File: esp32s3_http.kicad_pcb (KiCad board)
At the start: 2 copper layers, 55 x 90 mm, 30 parts, among them J1 USB_B, J2 Jack-DC, SW1 SW_Push, SW2 SW_Push, U1 ESP32-S3-WROOM-1, U2 LF33_TO220, U3 LF50_TO220, Y1 32.768KHz

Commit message: PCB: 回路図から更新 (F8, KiCad GUI)
Co-Authored-By: Claude Opus 5.5 <noreply@anthropic.com>
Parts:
- added J3: UART0, Connector_PinHeader_2.54mm:PinHeader_1x03_P2.54mm_Vertical, F.Cu at (88.5, 103.5)
- C1: value 22uF -> 22uF/10V; footprint Capacitor_SMD:C_0603_1608Metric_Pad1.08x0.95mm_HandSolder -> Capacitor_SMD:C_0805_2012Metric_Pad1.18x1.45mm_HandSolder
- C8: value 3.3uF -> 47uF/10V Ta; footprint Capacitor_SMD:C_0603_1608Metric_Pad1.08x0.95mm_HandSolder -> Capacitor_Tantalum_SMD:CP_EIA-3528-21_Kemet-B_HandSolder
- D1, D2, D3: value D -> 1N5819; footprint Diode_SMD:D_0603_1608Metric_Pad1.05x0.95mm_HandSolder -> Diode_THT:D_DO-41_SOD81_P7.62mm_Horizontal
- U2: value LF33_TO220 -> LM2940T-3.3
- U3: value LF50_TO220 -> NJM7805FA; footprint Package_TO_SOT_THT:TO-220-3_Vertical -> Package_TO_SOT_THT:TO-220F-3_Vertical
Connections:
- C8 pad 1: GND -> VDD33
- C8 pad 2: VDD33 -> GND
- U1 pad 15: SD_CS -> unconnected-(U1-IO3-Pad15)
- U1 pad 16: SD_SCK -> unconnected-(U1-IO46-Pad16)
- U1 pad 17: SD_MOSI -> SD_CS
- U1 pad 18: SD_MISO -> SD_SCK
- U1 pad 19: unconnected-(U1-IO11-Pad19) -> SD_MOSI
- U1 pad 20: unconnected-(U1-IO12-Pad20) -> SD_MISO
- U1 pad 36: unconnected-(U1-RXD0-Pad36) -> U0RXD
- U1 pad 37: unconnected-(U1-TXD0-Pad37) -> U0TXD

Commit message: PCB: 配置見直し、Freerouting による初回配線 (WIP)
Co-Authored-By: Claude Opus 5.5 <noreply@anthropic.com>
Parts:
- moved U6 45.6 mm to (60.5, 142.9), turned to 180 degrees
- moved D1 14.7 mm to (68.6, 121.5)
- moved U3 9.06 mm to (63.1, 122.6), turned to 180 degrees
- moved C9 8.94 mm to (63.6, 119.3), turned to 0 degrees
- moved D2 7.74 mm to (64.0, 112.3)
- moved C4 7.23 mm to (57.5, 109.3), turned to 0 degrees
- moved C8 6.74 mm to (68.5, 109.5)
- moved D3 6.43 mm to (64.0, 116.3), turned to 180 degrees
- moved C10 5.86 mm to (57.5, 119.3)
- moved H2 4.96 mm to (89.0, 68.6)
- moved U2 4.94 mm to (58.5, 106.0)
- moved J3 1.06 mm to (89.6, 103.5)
- renumbered REF** to H1, REF** to H2, REF** to H3, REF** to H4
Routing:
- net BOOT: track 53.4 -> 72.3 mm
- net JACK5V: track 25.8 -> 7.27 mm
- net Net-(D1-K): track 24.8 -> 9.85 mm
- net Net-(D1-A): track 4.75 -> 17.7 mm
- net W5500_CS: track 37.9 -> 44.5 mm, vias 0 -> 1
- net U0TXD: track 0.00 -> 5.56 mm
- net EN: track 52.3 -> 46.9 mm, vias 2 -> 0
- net U0RXD: track 0.00 -> 4.95 mm
- net 5V: track 42.4 -> 37.8 mm
- net SD_MOSI: track 35.5 -> 32.8 mm
- net SD_MISO: track 34.9 -> 32.2 mm
- net SD_SCK: track 35.8 -> 33.4 mm
- net DM: track 39.6 -> 42.0 mm, vias 0 -> 1
- net VDD33: track 96.5 -> 98.7 mm, vias 2 -> 0
- net W5500_NT: track 34.0 -> 36.1 mm, vias 0 -> 1
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
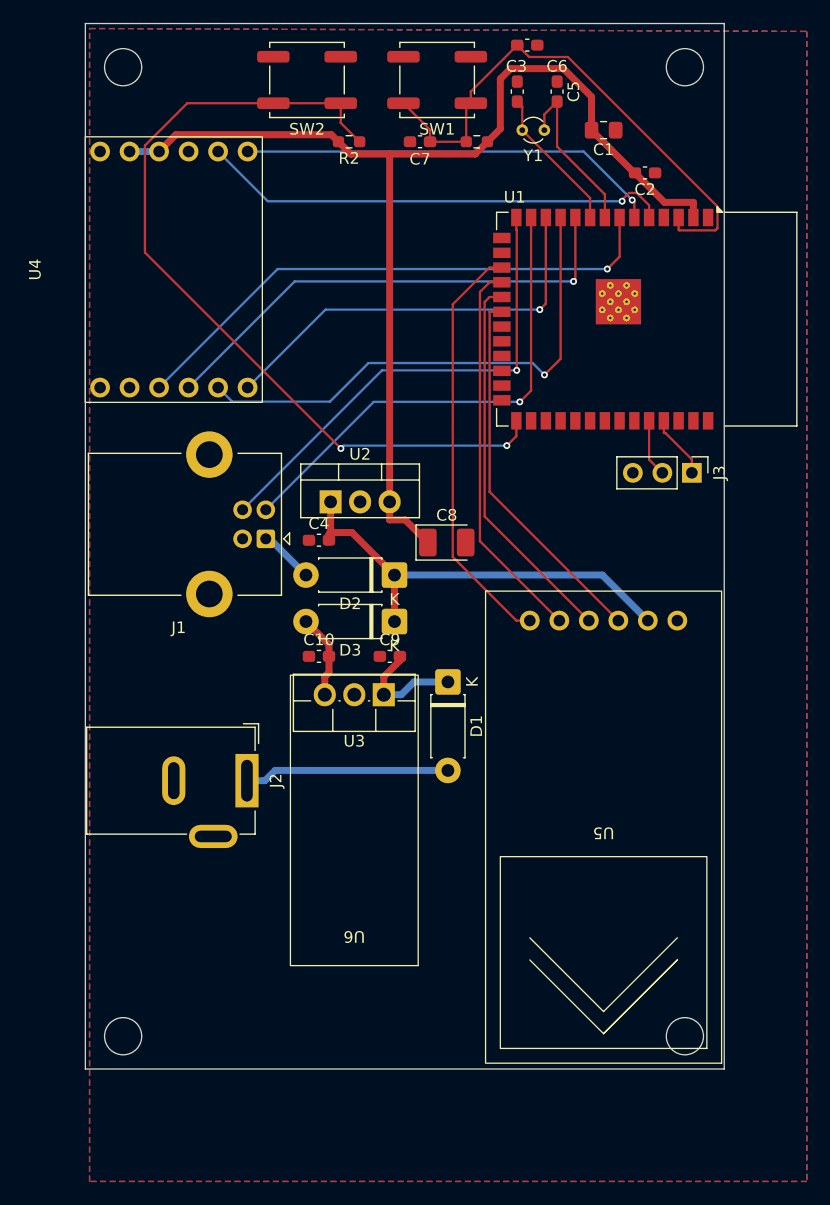
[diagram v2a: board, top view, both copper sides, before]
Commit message: PCB: W5500/SD のピン割当を配線向きに変更、EN/デカップリング集約、GND ステッチング
- W5500: IO9-IO14 (U1 左辺), SD: IO38-IO41 (U1 下辺, U5 直上)
- C2 を U1 pin1/2 直上に、EN 回路を pin3 直上に集約
- U1 EPAD サーマルビア 0.2 -> 0.3mm
- Power/GND ネットクラス (0.6mm) 追加

Co-Authored-By: Claude Opus 5.5 <noreply@anthropic.com>
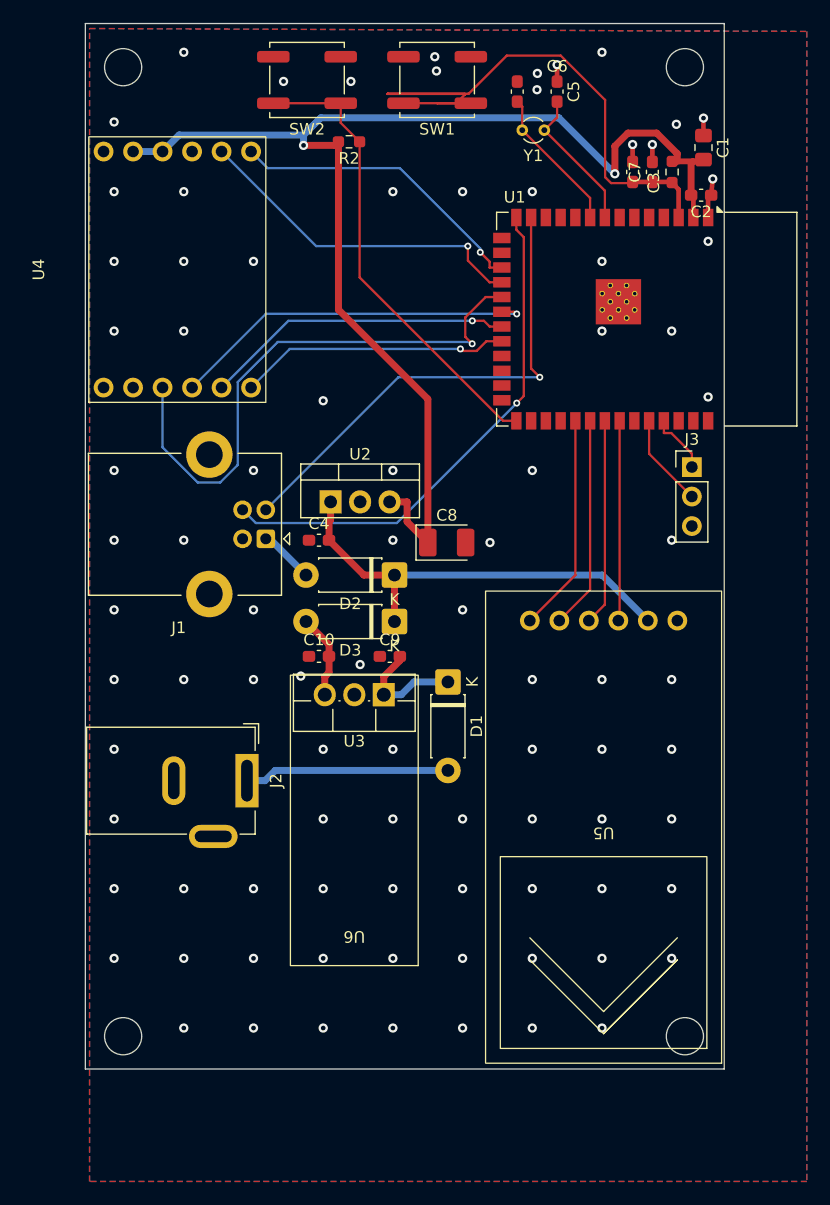
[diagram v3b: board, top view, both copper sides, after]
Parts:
- moved C7 20.2 mm to (86.2, 77.6), turned to -90 degrees
- moved R1 17.0 mm to (87.9, 77.6), turned to -90 degrees
- moved C3 14.2 mm to (84.5, 77.6), turned to -90 degrees
- moved C1 8.73 mm to (90.6, 75.5), turned to -90 degrees
- moved C2 5.20 mm to (90.4, 79.6)
- moved J3 0.50 mm to (89.6, 103.0), turned to 0 degrees
- moved U4 0.30 mm to (33.9, 86.0)
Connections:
- U1 pad 10: W5500_SCK -> unconnected-(U1-IO17-Pad10)
- U1 pad 11: W5500_CS -> unconnected-(U1-IO18-Pad11)
- U1 pad 12: W5500_NT -> unconnected-(U1-IO8-Pad12)
- U1 pad 17: SD_CS -> W5500_MOSI
- U1 pad 18: SD_SCK -> W5500_RST
- U1 pad 19: SD_MOSI -> W5500_MISO
- U1 pad 20: SD_MISO -> W5500_SCK
- U1 pad 21: unconnected-(U1-IO13-Pad21) -> W5500_CS
- U1 pad 22: unconnected-(U1-IO14-Pad22) -> W5500_NT
- U1 pad 31: unconnected-(U1-IO38-Pad31) -> SD_CS
- U1 pad 32: unconnected-(U1-IO39-Pad32) -> SD_SCK
- U1 pad 33: unconnected-(U1-IO40-Pad33) -> SD_MOSI
- U1 pad 34: unconnected-(U1-IO41-Pad34) -> SD_MISO
- U1 pad 5: W5500_RST -> unconnected-(U1-IO5-Pad5)
- U1 pad 6: W5500_MOSI -> unconnected-(U1-IO6-Pad6)
- U1 pad 7: W5500_MISO -> unconnected-(U1-IO7-Pad7)
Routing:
- net BOOT: track 72.3 -> 40.1 mm, vias 2 -> 0
- net W5500_CS: track 44.5 -> 26.7 mm
- net SD_CS: track 36.2 -> 18.8 mm
- net SD_SCK: track 33.4 -> 18.3 mm
- net SD_MOSI: track 32.8 -> 17.8 mm
- net SD_MISO: track 32.2 -> 17.2 mm
- net W5500_NT: track 36.1 -> 23.4 mm
- net W5500_RST: track 40.7 -> 29.5 mm
- net VDD33: track 98.7 -> 109.7 mm, vias 0 -> 2
- net W5500_SCK: track 42.5 -> 31.9 mm
- net W5500_MOSI: track 36.4 -> 26.2 mm
- net GND: track 0.00 -> 9.54 mm, vias 0 -> 89
- net EN: track 46.9 -> 54.5 mm
- net DP: track 41.7 -> 44.8 mm
- net U0RXD: track 4.95 -> 8.04 mm
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
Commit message: PCB: 配線完了、シルク整理
- W5500 バス・VDD33 幹線・EN/デカップリングを固定配線、残りを Freerouting で配線
- GND ステッチングビア、値表示を F.Fab へ、リファレンス位置調整
- DRC: 未配線 0、電気的違反 0 (残りは U3/U6 重ね置き等の意図的なもの)

Co-Authored-By: Claude Opus 5.5 <noreply@anthropic.com>
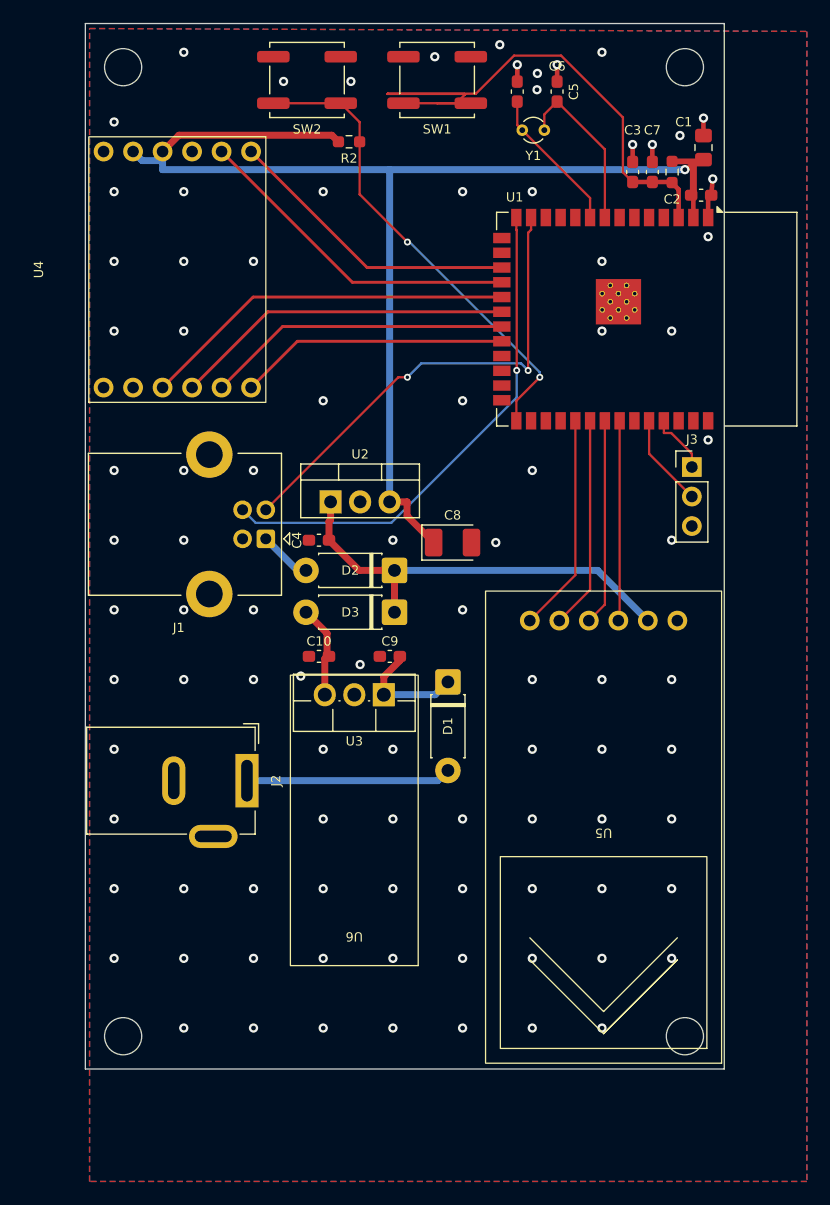
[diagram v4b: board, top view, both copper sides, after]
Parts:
- moved D3 0.80 mm to (64.0, 115.5)
- moved C8 0.50 mm to (69.0, 109.5)
- moved D2 0.40 mm to (64.0, 111.9)
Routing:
- net W5500_MISO: track 48.7 -> 32.4 mm, vias 1 -> 0
- net EN: track 54.5 -> 51.6 mm
- net W5500_SCK: track 31.9 -> 29.4 mm, vias 1 -> 0
- net Net-(U1-IO15): track 12.6 -> 14.6 mm
- net GND: track 9.54 -> 11.0 mm, vias 89 -> 92
- net BOOT: track 40.1 -> 41.2 mm, vias 0 -> 2
- net DM: track 42.4 -> 41.3 mm, vias 1 -> 2
- net JACK5V: track 7.27 -> 8.10 mm
- net DP: track 44.8 -> 44.0 mm
- net W5500_RST: track 29.5 -> 28.8 mm, vias 1 -> 0
- net W5500_MOSI: track 26.2 -> 25.7 mm, vias 1 -> 0
- net VDD33: track 109.7 -> 109.3 mm, vias 2 -> 1
- net W5500_CS: track 26.7 -> 26.3 mm, vias 1 -> 0
- net W5500_NT: track 23.4 -> 23.2 mm, vias 1 -> 0

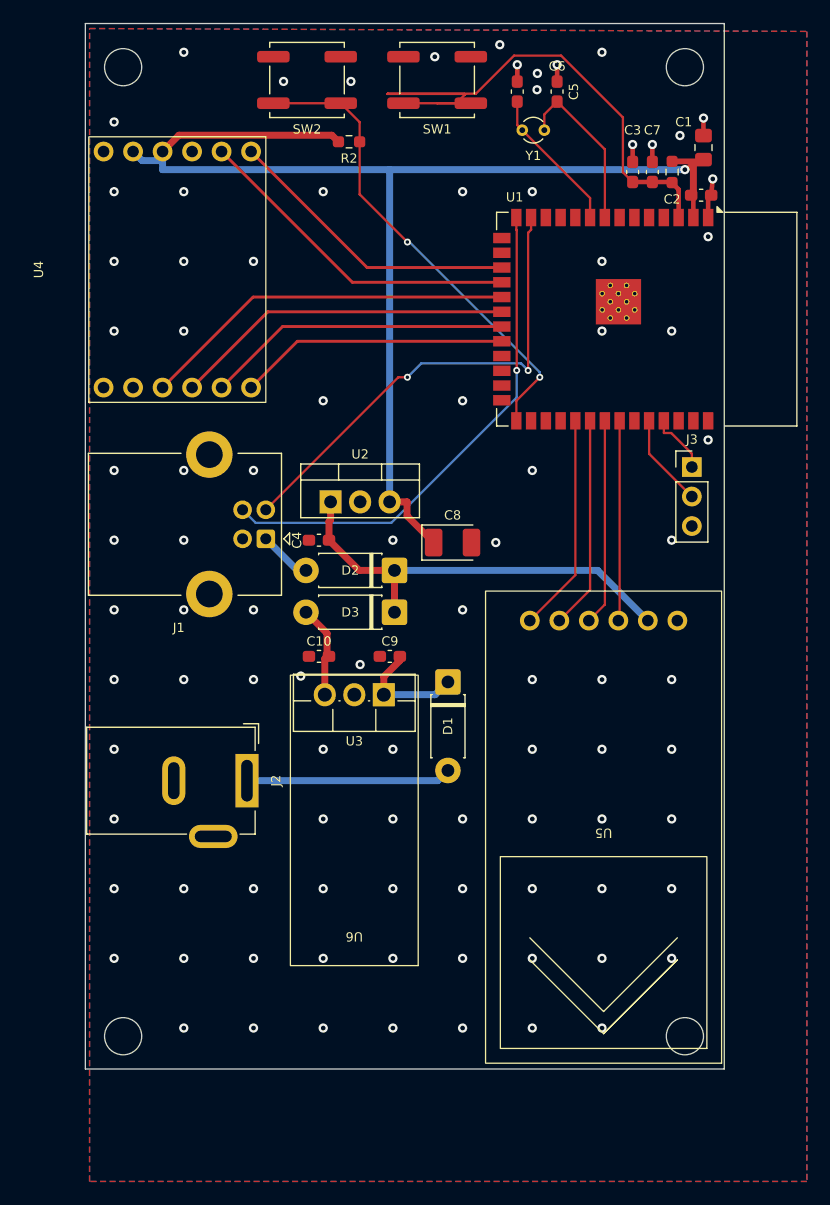
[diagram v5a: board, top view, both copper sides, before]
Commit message: PCB: OS-CON 1000uF (C11: W5500 給電点, C12: LM2940 出力/ESP32 幹線起点) を追加
Co-Authored-By: Claude Opus 5.5 <noreply@anthropic.com>
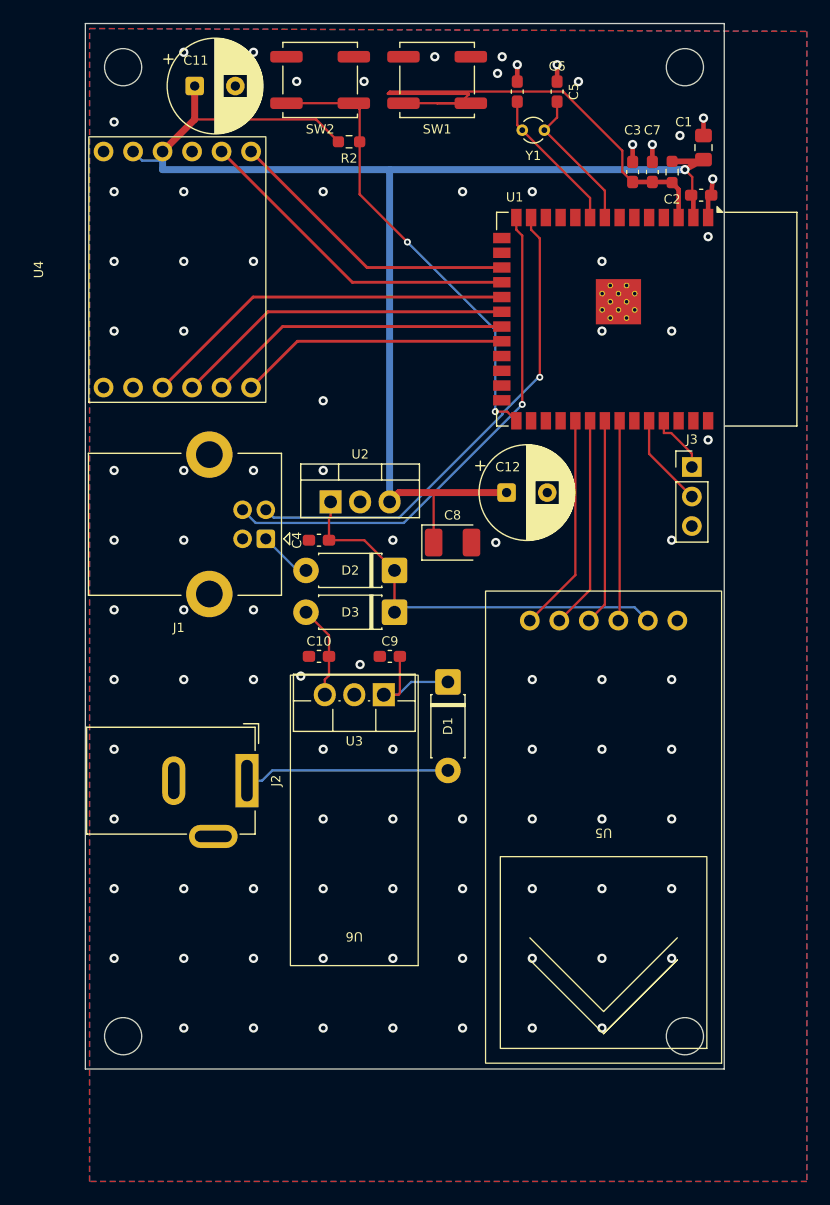
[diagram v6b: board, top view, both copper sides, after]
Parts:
- added C11: 1000uF/6.3V OS-CON, Capacitor_THT:CP_Radial_D8.0mm_P3.50mm, F.Cu at (46.8, 70.2)
- added C12: 1000uF/6.3V OS-CON, Capacitor_THT:CP_Radial_D8.0mm_P3.50mm, F.Cu at (73.7, 105.2)
- moved SW2 1.13 mm to (57.6, 69.7)
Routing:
- net VDD33: track 109.3 -> 121.9 mm
- net EN: track 51.6 -> 48.0 mm
- net Net-(U1-IO15): track 14.6 -> 12.6 mm
- net BOOT: track 41.2 -> 39.5 mm
- net DM: track 41.3 -> 43.0 mm, vias 2 -> 1
- net 5V: track 37.3 -> 36.1 mm
- net DP: track 44.0 -> 45.1 mm
- net Net-(D1-K): track 9.85 -> 10.6 mm
- net GND: vias 92 -> 91

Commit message: PCB: 動作確認用 LED を追加
- PWR/3V3/STAT を左端パネルに、LAN は W5500 バス下、SD は U5 横に配置
- LAN/SD は VDD33→LED→R→CS 構成 (アノードを近傍の VDD33 に直結)

Co-Authored-By: Claude Opus 5.5 <noreply@anthropic.com>
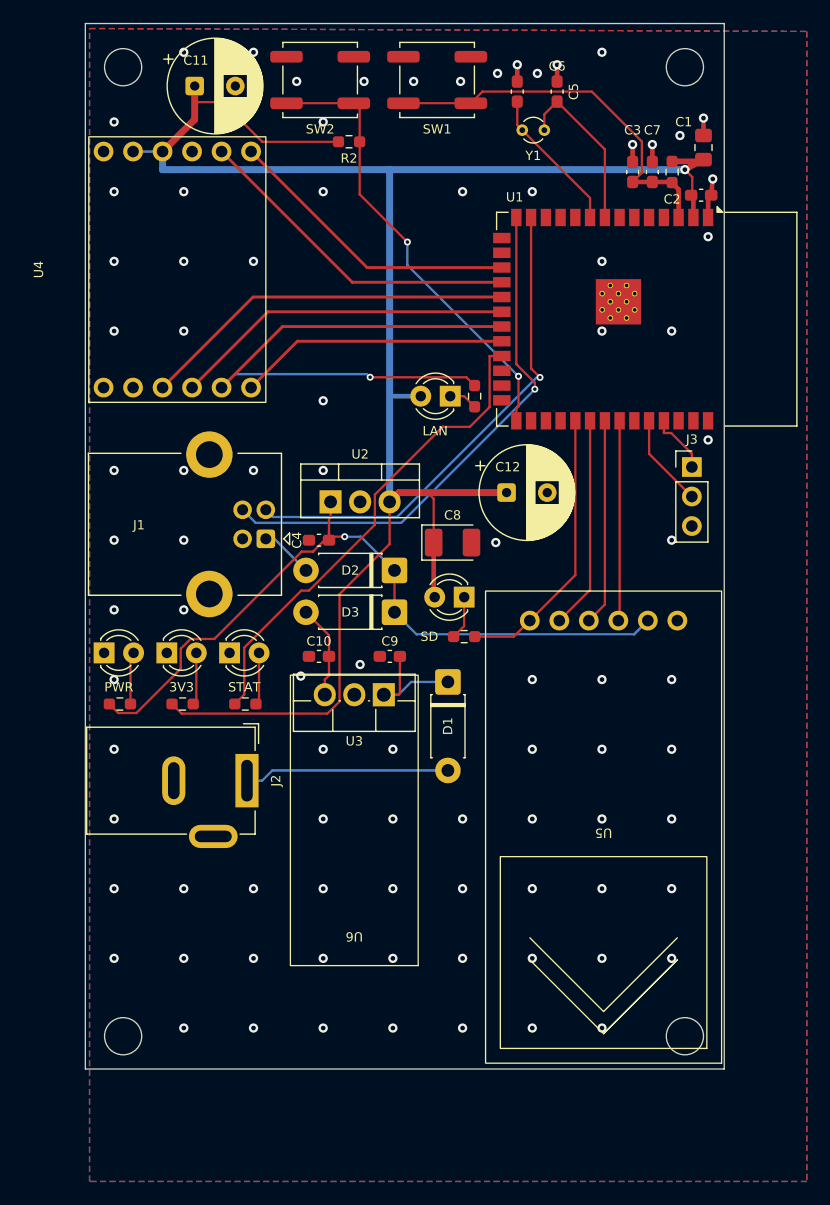
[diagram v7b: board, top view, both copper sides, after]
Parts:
- added D4: Red, LED_THT:LED_D3.0mm, F.Cu at (39.0, 119.0)
- added D5: Green, LED_THT:LED_D3.0mm, F.Cu at (44.4, 119.0)
- added D6: Yellow, LED_THT:LED_D3.0mm, F.Cu at (49.8, 119.0)
- added D7: Orange, LED_THT:LED_D3.0mm, F.Cu at (68.8, 96.9)
- added D8: Orange, LED_THT:LED_D3.0mm, F.Cu at (70.0, 114.2)
- added R4: 2.2k, Resistor_SMD:R_0603_1608Metric_Pad0.98x0.95mm_HandSolder, F.Cu at (40.4, 123.4)
- added R5: 1k, Resistor_SMD:R_0603_1608Metric_Pad0.98x0.95mm_HandSolder, F.Cu at (45.8, 123.4)
- added R6: 1k, Resistor_SMD:R_0603_1608Metric_Pad0.98x0.95mm_HandSolder, F.Cu at (51.2, 123.4)
- added R7: 1k, Resistor_SMD:R_0603_1608Metric_Pad0.98x0.95mm_HandSolder, F.Cu at (70.9, 96.9)
- added R8: 1k, Resistor_SMD:R_0603_1608Metric_Pad0.98x0.95mm_HandSolder, F.Cu at (70.0, 117.6)
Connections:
- U1 pad 23: unconnected-(U1-IO21-Pad23) -> LED_STAT
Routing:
- net VDD33: track 121.9 -> 164.0 mm
- net LED_STAT: track 0.00 -> 41.9 mm
- net 5V: track 36.1 -> 64.0 mm, vias 0 -> 1
- net W5500_CS: track 26.3 -> 49.0 mm, vias 0 -> 1
- net EN: track 48.0 -> 33.2 mm
- net SD_CS: track 18.8 -> 24.1 mm
- net Net-(D6-A): track 0.00 -> 4.51 mm
- net Net-(D5-A): track 0.00 -> 4.51 mm
- net Net-(D4-A): track 0.00 -> 4.51 mm
- net Net-(D8-K): track 0.00 -> 3.78 mm
- net Net-(D7-K): track 0.00 -> 2.49 mm
- net Net-(U1-IO15): track 12.6 -> 14.6 mm
- net DP: track 45.1 -> 45.8 mm
- net GND: vias 91 -> 89
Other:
- board text added: "3V3"
- board text added: "LAN"
- board text added: "PWR"
- board text added: "SD"
- board text added: "STAT"
